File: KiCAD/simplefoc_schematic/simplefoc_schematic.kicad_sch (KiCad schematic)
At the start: 75 parts, among them IC1 TMC6140-Trinamic, J1 Power Supply, J2 Motor Connector, J3 Sensor Connector, J5 Programming Port, J6 UART Port, J7 Servo, Q1 IRLR 2905, Q2 IRLR 2905, Q3 IRLR 2905, Q4 IRLR 2905, Q5 IRLR 2905, Q6 IRLR 2905, SW1 SW_Push, U1 MC7805CDTG, U2 STM32F101CBT6

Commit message: Minor changes to power tracks
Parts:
- gave numbers to parts that had none: 4
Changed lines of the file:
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@@
   (symbol (lib_id "Connector:TestPoint") (at 160.02 214.63 0) (unit 1)
     (in_bom yes) (on_board yes) (fields_autoplaced)
-    (property "Reference" "TP?" (id 0) (at 161.417 210.4933 0)
+    (property "Reference" "TP7" (id 0) (at 161.417 210.4933 0)
       (effects (font (size 1.27 1.27)) (justify left))
     )
@@
   (symbol (lib_id "Connector:TestPoint") (at 146.05 214.63 0) (unit 1)
     (in_bom yes) (on_board yes) (fields_autoplaced)
-    (property "Reference" "TP?" (id 0) (at 147.447 210.4933 0)
+    (property "Reference" "TP3" (id 0) (at 147.447 210.4933 0)
       (effects (font (size 1.27 1.27)) (justify left))
     )
@@
   (symbol (lib_id "Connector:TestPoint") (at 185.42 214.63 0) (unit 1)
     (in_bom yes) (on_board yes) (fields_autoplaced)
-    (property "Reference" "TP?" (id 0) (at 186.817 210.4933 0)
+    (property "Reference" "TP9" (id 0) (at 186.817 210.4933 0)
       (effects (font (size 1.27 1.27)) (justify left))
     )
@@
   (symbol (lib_id "Connector:TestPoint") (at 172.72 214.63 0) (unit 1)
     (in_bom yes) (on_board yes) (fields_autoplaced)
-    (property "Reference" "TP?" (id 0) (at 174.117 210.4933 0)
+    (property "Reference" "TP8" (id 0) (at 174.117 210.4933 0)
       (effects (font (size 1.27 1.27)) (justify left))
     )
@@
       (reference "TP2") (unit 1) (value "TestPoint") (footprint "TestPoint:TestPoint_Pad_1.5x1.5mm")
     )
+    (path "/3019c608-0d77-49cc-9c3f-99fc2de14958"
+      (reference "TP3") (unit 1) (value "TestPoint") (footprint "TestPoint:TestPoint_Pad_D1.0mm")
+    )
     (path "/d53a2018-3628-433f-89b8-76ef79b0d900"
       (reference "TP4") (unit 1) (value "TestPoint") (footprint "TestPoint:TestPoint_Pad_1.5x1.5mm")
@@
     )
     (path "/06166001-b06f-403d-8b44-3d5438f7b61c"
-      (reference "TP?") (unit 1) (value "TestPoint") (footprint "TestPoint:TestPoint_Pad_D1.0mm")
-    )
-    (path "/3019c608-0d77-49cc-9c3f-99fc2de14958"
-      (reference "TP?") (unit 1) (value "TestPoint") (footprint "TestPoint:TestPoint_Pad_D1.0mm")
+      (reference "TP7") (unit 1) (value "TestPoint") (footprint "TestPoint:TestPoint_Pad_D1.0mm")
+    )
+    (path "/b1d9a51c-b366-4be0-b1da-3925c052c783"
+      (reference "TP8") (unit 1) (value "TestPoint") (footprint "TestPoint:TestPoint_Pad_D1.0mm")
     )
     (path "/366ba791-2b9f-4771-8751-9001ebd2b43e"
-      (reference "TP?") (unit 1) (value "TestPoint") (footprint "TestPoint:TestPoint_Pad_D1.0mm")
-    )
-    (path "/b1d9a51c-b366-4be0-b1da-3925c052c783"
-      (reference "TP?") (unit 1) (value "TestPoint") (footprint "TestPoint:TestPoint_Pad_D1.0mm")
+      (reference "TP9") (unit 1) (value "TestPoint") (footprint "TestPoint:TestPoint_Pad_D1.0mm")
     )
     (path "/4130870a-0c86-40cf-99a0-88504ab08dfb"

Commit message: First design of the final small PCB
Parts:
- removed C22: 100nF/35V, Capacitor_SMD:C_0603_1608Metric, symbol Device:C_Small
- removed C28, C29, C31: 1000uF/25V, Capacitor_SMD:CP_Elec_10x14.3, symbol Device:C_Polarized_Small
- removed D1, D2: D_Schottky, Additional_Components:DIODE_MSS1P4-M3_89A, symbol Device:D_Schottky
- removed R10: 0R, Resistor_SMD:R_0603_1608Metric, symbol Device:R_Small
- removed TP1, TP2, TP4, TP5, TP6: TestPoint, TestPoint:TestPoint_Pad_1.5x1.5mm, symbol Connector:TestPoint
- removed TP3, TP7, TP8, TP9: TestPoint, TestPoint:TestPoint_Pad_D1.0mm, symbol Connector:TestPoint
- C30: value 1000uF/25V -> 220uF/25V; footprint Capacitor_SMD:CP_Elec_10x14.3 -> Capacitor_SMD:CP_Elec_8x10
- H1, H2, H3, H4: footprint MountingHole:MountingHole_2.5mm_Pad -> MountingHole:MountingHole_2.2mm_M2_DIN965_Pad
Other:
- note added: "Zu Beschaffen: - TMC6140 - 10uF 25v 0603 - 22uF 6.3v 0603 - MSS1P6"
- note removed: "Only close when VS < 15V"
- note removed: "TODO:"

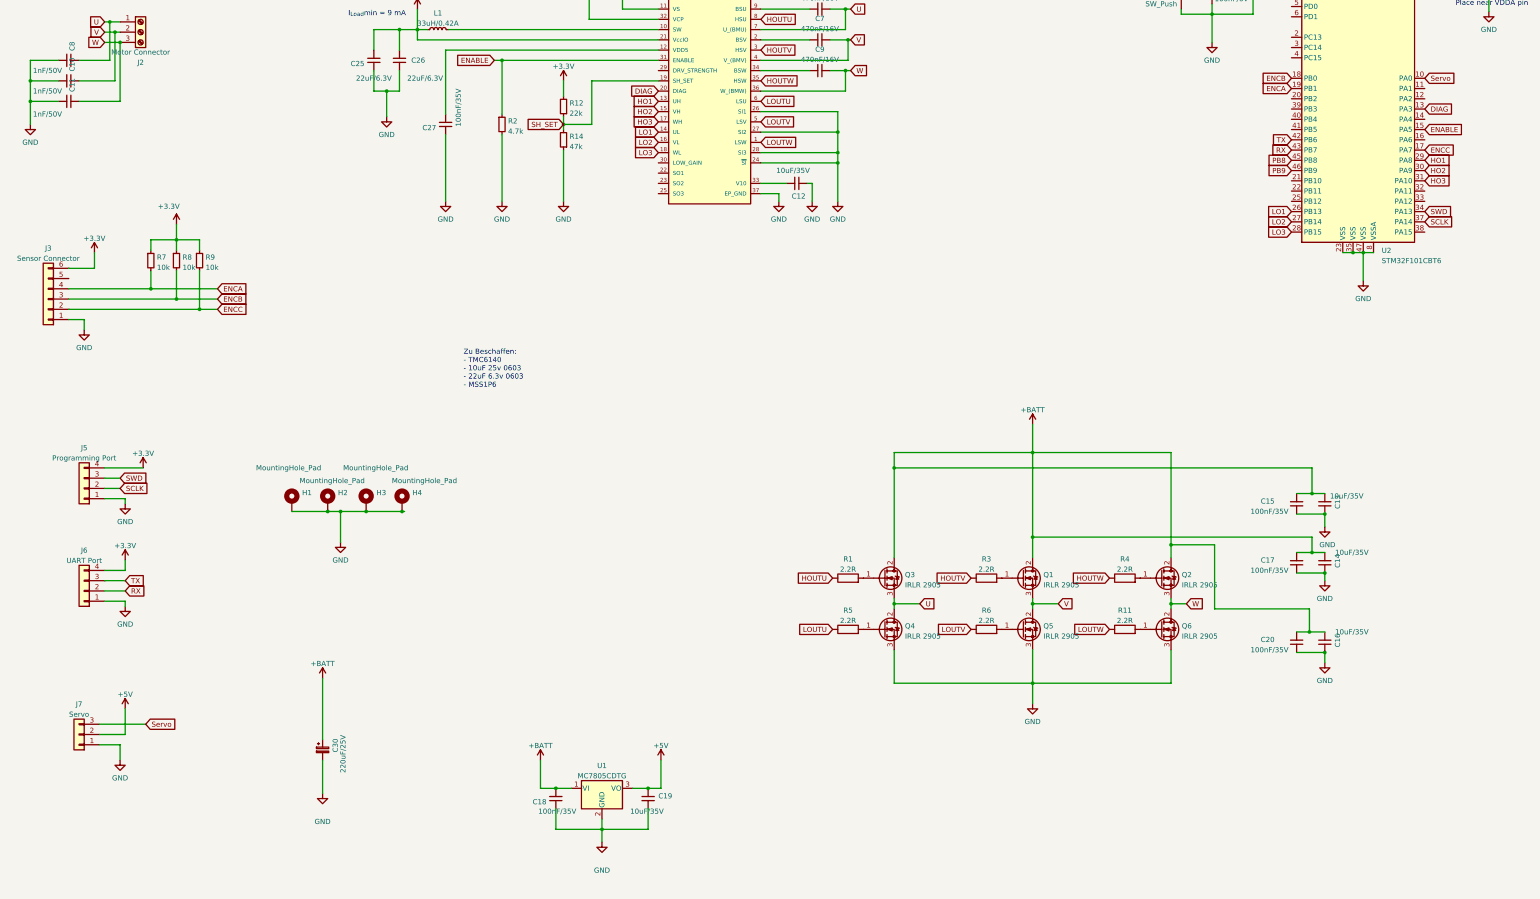
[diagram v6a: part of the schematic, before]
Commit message: Added second servo connection and fuse for servo
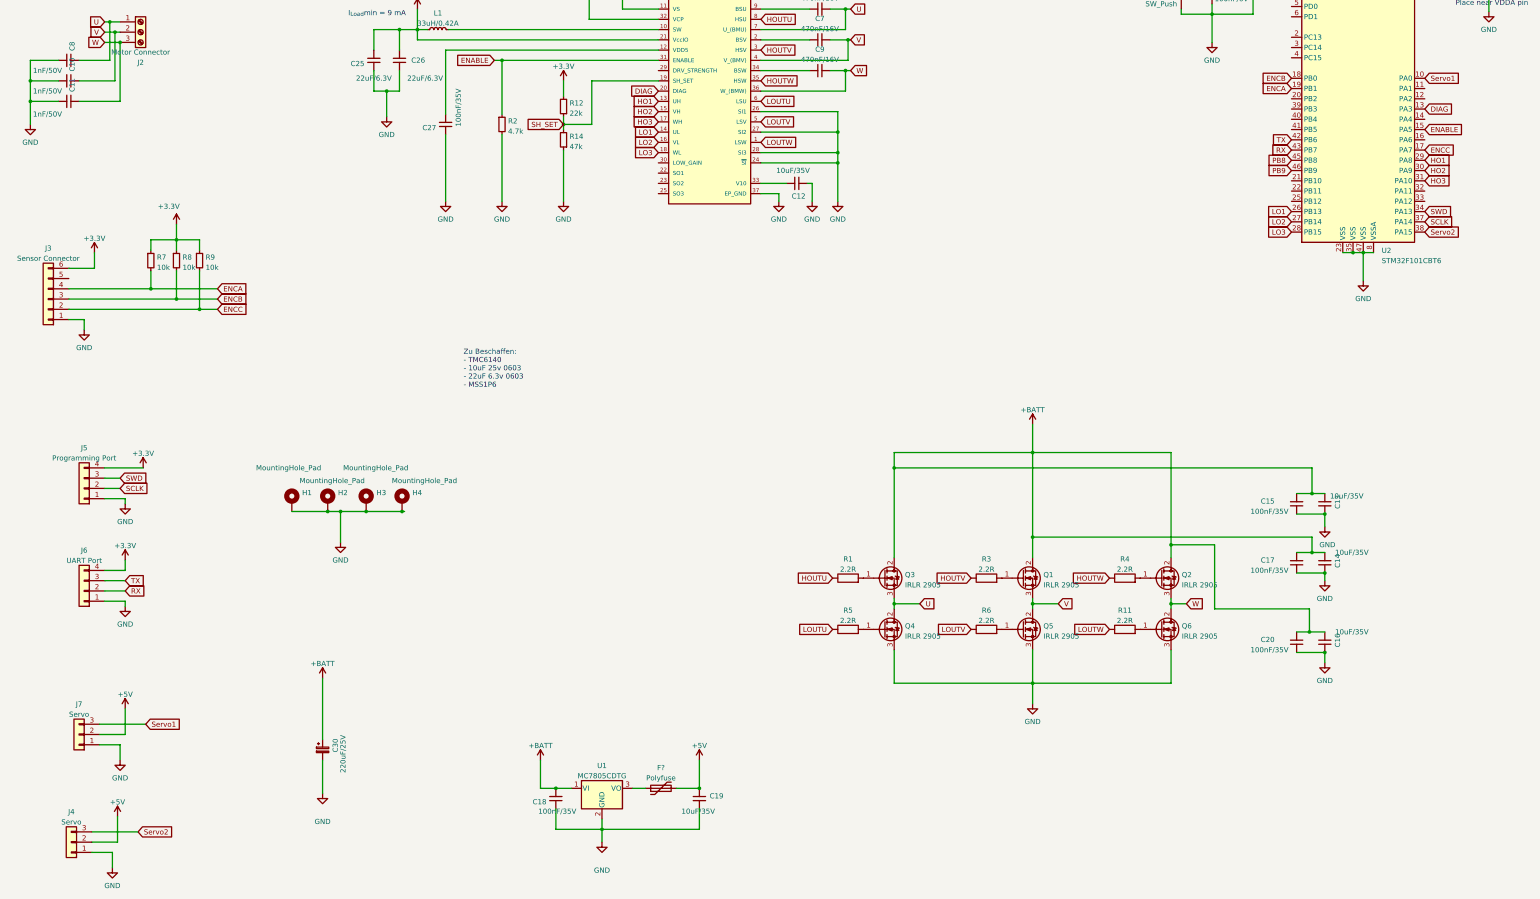
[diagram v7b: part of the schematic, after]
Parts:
- added F?: Polyfuse, Resistor_SMD:R_0603_1608Metric_Pad0.98x0.95mm_HandSolder, symbol Device:Polyfuse
- added J4: Servo, Connector_PinSocket_2.54mm:PinSocket_1x03_P2.54mm_Vertical, symbol Connector_Generic:Conn_01x03
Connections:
- net +5V: now also F?.2, J4.2 (Pin_2); no longer U1.3 (VO)
- net GND: now also J4.1 (Pin_1)
- net Servo2: now reaches U2.38 (PA15)
- net Servo2: now also J4.3 (Pin_3)
- net Servo renamed Servo1
- new net: F?.1, U1.3 (VO)
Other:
- moved on the sheet: C19

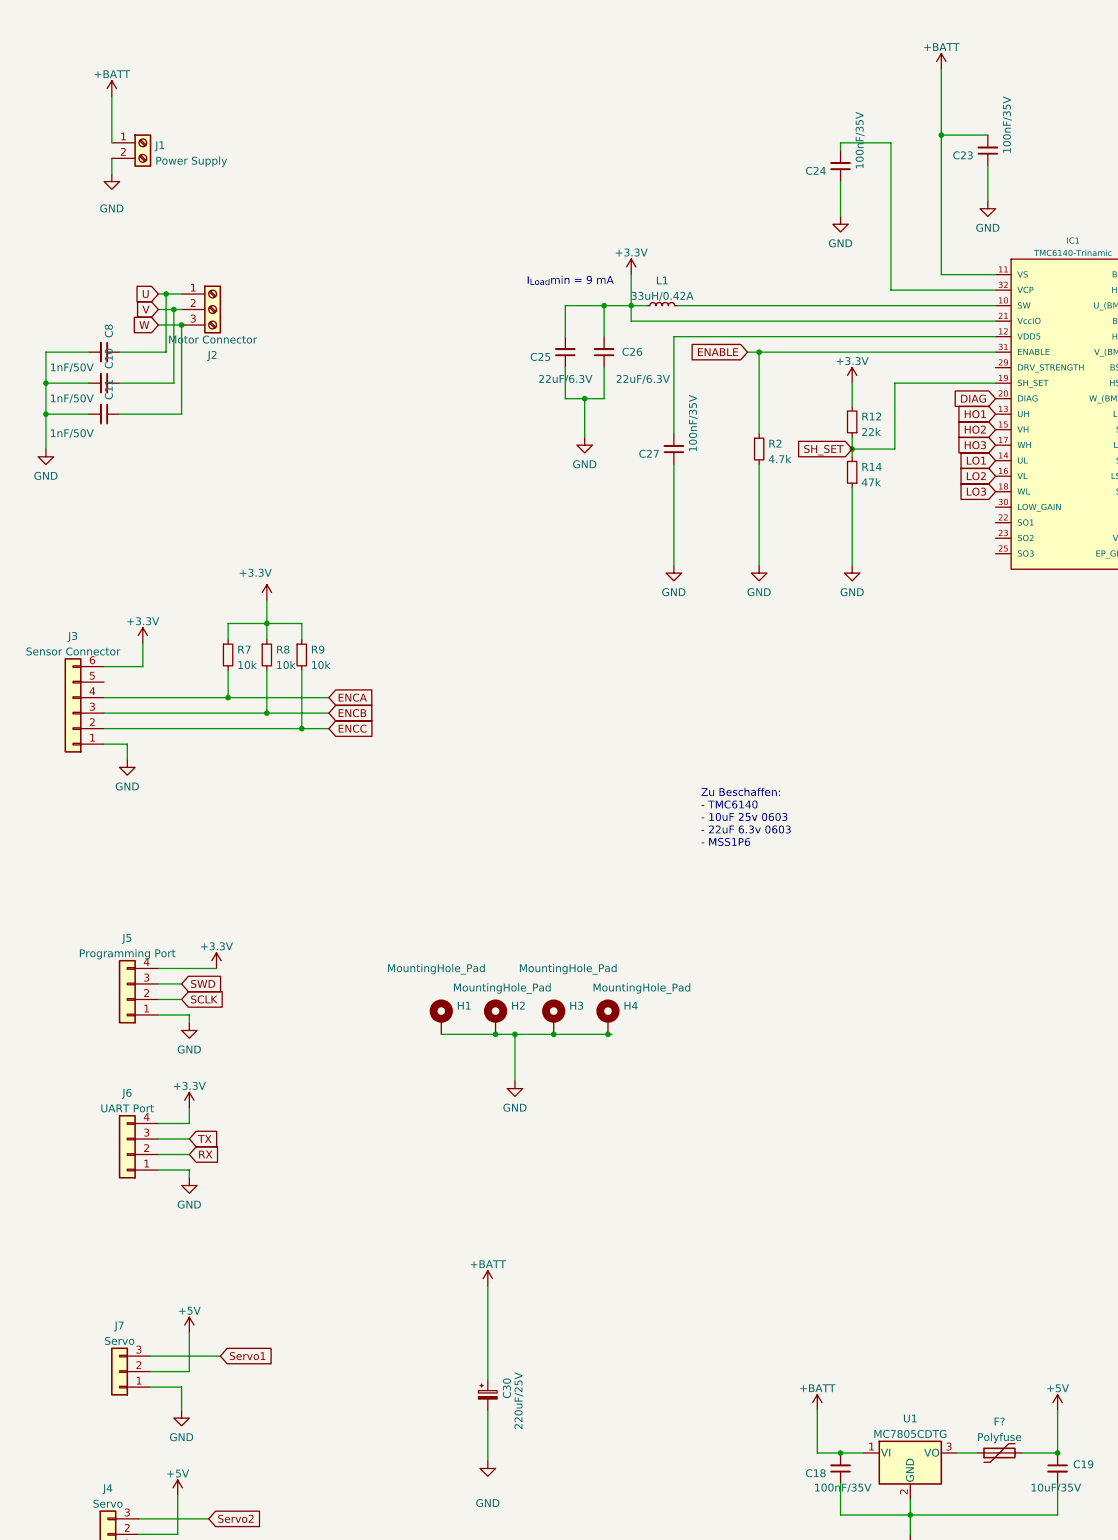
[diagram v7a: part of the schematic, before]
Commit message: Added polyfuse to battery input
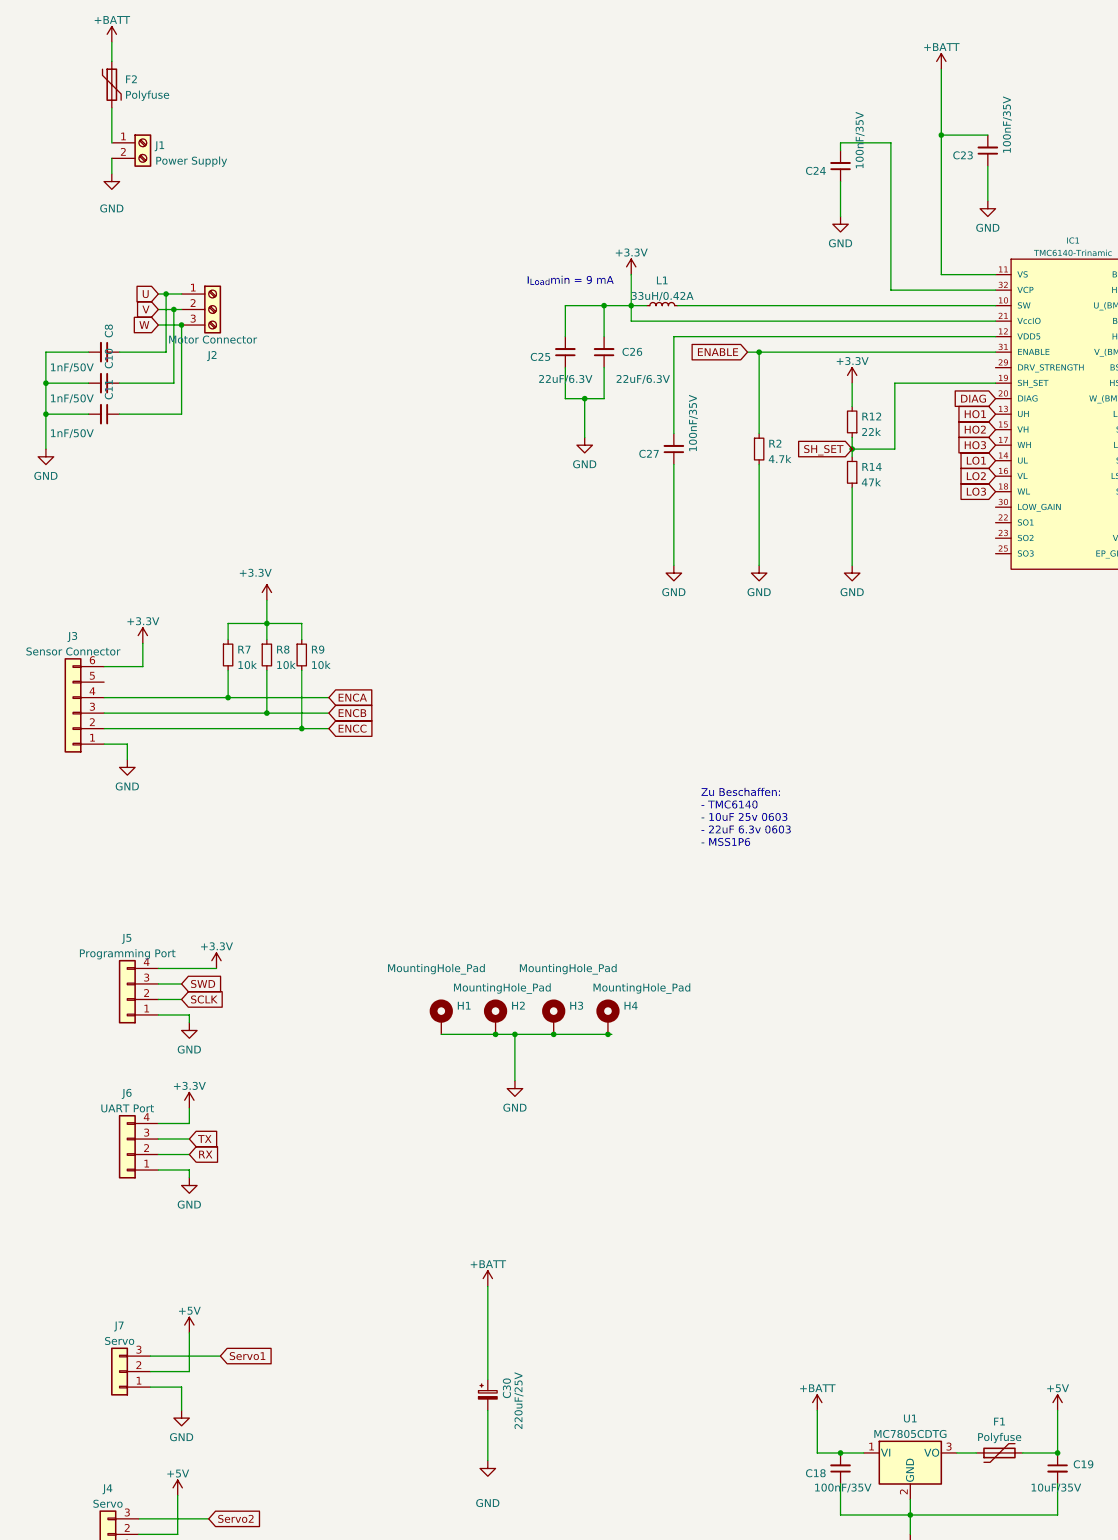
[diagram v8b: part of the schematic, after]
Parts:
- added F2: Polyfuse, Fuse:Fuse_2920_7451Metric_Pad2.10x5.45mm_HandSolder, symbol Device:Polyfuse
- F1: renamed from F?; footprint Resistor_SMD:R_0603_1608Metric_Pad0.98x0.95mm_HandSolder -> Fuse:Fuse_0603_1608Metric_Pad1.05x0.95mm_HandSolder
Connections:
- net +BATT: now also F2.1; no longer J1.1 (Pin_1)
- new net: F2.2, J1.1 (Pin_1)
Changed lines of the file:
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@@
-    (stroke (width 0) (type default) (color 0 0 0 0))
-  )
-  (wire (pts (xy 31.75 29.21) (xy 31.75 36.83))
     (stroke (width 0) (type default) (color 0 0 0 0))
   )
@@
     (stroke (width 0) (type default) (color 0 0 0 0))
   )
+  (wire (pts (xy 31.75 20.32) (xy 31.75 23.495))
+    (stroke (width 0) (type default) (color 0 0 0 0))
+  )
   (wire (pts (xy 314.325 191.135) (xy 303.53 191.135))
     (stroke (width 0) (type default) (color 0 0 0 0))
@@
   )
   (wire (pts (xy 334.645 193.04) (xy 338.455 193.04))
+    (stroke (width 0) (type default) (color 0 0 0 0))
+  )
+  (wire (pts (xy 31.75 31.115) (xy 31.75 36.83))
     (stroke (width 0) (type default) (color 0 0 0 0))
   )
@@
   (symbol (lib_id "Device:Polyfuse") (at 177.165 251.46 90) (unit 1)
     (in_bom yes) (on_board yes) (fields_autoplaced)
-    (property "Reference" "F?" (id 0) (at 177.165 246.3632 90))
+    (property "Reference" "F1" (id 0) (at 177.165 246.3632 90))
     (property "Value" "Polyfuse" (id 1) (at 177.165 248.9001 90))
-    (property "Footprint" "Resistor_SMD:R_0603_1608Metric_Pad0.98x0.95mm_HandSolder" (id 2) (at 182.245 250.19 0)
+    (property "Footprint" "Fuse:Fuse_0603_1608Metric_Pad1.05x0.95mm_HandSolder" (id 2) (at 182.245 250.19 0)
       (effects (font (size 1.27 1.27)) (justify left) hide)
     )
@@
     )
     (pin "1")
+  )
+  (symbol (lib_id "Device:Polyfuse") (at 31.75 27.305 0) (unit 1)
+    (in_bom yes) (on_board yes) (fields_autoplaced)
+    (property "Reference" "F2" (id 0) (at 33.909 26.4703 0)
+      (effects (font (size 1.27 1.27)) (justify left))
+    )
+    (property "Value" "Polyfuse" (id 1) (at 33.909 29.0072 0)
+      (effects (font (size 1.27 1.27)) (justify left))
+    )
+    (property "Footprint" "Fuse:Fuse_2920_7451Metric_Pad2.10x5.45mm_HandSolder" (id 2) (at 33.02 32.385 0)
+      (effects (font (size 1.27 1.27)) (justify left) hide)
+    )
+    (property "Datasheet" "~" (id 3) (at 31.75 27.305 0)
+      (effects (font (size 1.27 1.27)) hide)
+    )
+    (pin "1")
+    (pin "2")
   )
   (symbol (lib_id "power:GND") (at 220.98 106.045 0) (unit 1)
@@
     (pin "2")
   )
-  (symbol (lib_id "power:+BATT") (at 31.75 29.21 0) (unit 1)
-    (in_bom yes) (on_board yes) (fields_autoplaced)
-    (property "Reference" "#PWR0108" (id 0) (at 31.75 33.02 0)
-      (effects (font (size 1.27 1.27)) hide)
-    )
-    (property "Value" "+BATT" (id 1) (at 31.75 25.6342 0))
-    (property "Footprint" "" (id 2) (at 31.75 29.21 0)
-      (effects (font (size 1.27 1.27)) hide)
-    )
-    (property "Datasheet" "" (id 3) (at 31.75 29.21 0)
+  (symbol (lib_id "power:+BATT") (at 31.75 20.32 0) (unit 1)
+    (in_bom yes) (on_board yes) (fields_autoplaced)
+    (property "Reference" "#PWR0108" (id 0) (at 31.75 24.13 0)
+      (effects (font (size 1.27 1.27)) hide)
+    )
+    (property "Value" "+BATT" (id 1) (at 31.75 16.7442 0))
+    (property "Footprint" "" (id 2) (at 31.75 20.32 0)
+      (effects (font (size 1.27 1.27)) hide)
+    )
+    (property "Datasheet" "" (id 3) (at 31.75 20.32 0)
       (effects (font (size 1.27 1.27)) hide)
     )
@@
     )
     (path "/09ae4ae7-95d4-4828-b6a2-176e4b4c1dd6"
-      (reference "F?") (unit 1) (value "Polyfuse") (footprint "Resistor_SMD:R_0603_1608Metric_Pad0.98x0.95mm_HandSolder")
+      (reference "F1") (unit 1) (value "Polyfuse") (footprint "Fuse:Fuse_0603_1608Metric_Pad1.05x0.95mm_HandSolder")
+    )
+    (path "/187994f7-20ff-443d-bc47-22a82ce88358"
+      (reference "F2") (unit 1) (value "Polyfuse") (footprint "Fuse:Fuse_2920_7451Metric_Pad2.10x5.45mm_HandSolder")
     )
     (path "/fba6a18d-63c5-4da7-badf-0bfe7adeb13a"
